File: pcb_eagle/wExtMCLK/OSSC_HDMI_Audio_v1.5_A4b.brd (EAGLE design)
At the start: 29.8 x 25.9 mm, 29 parts, among them U1 PCM1808, U2 74LVC1G34, U3 MK2507SLF

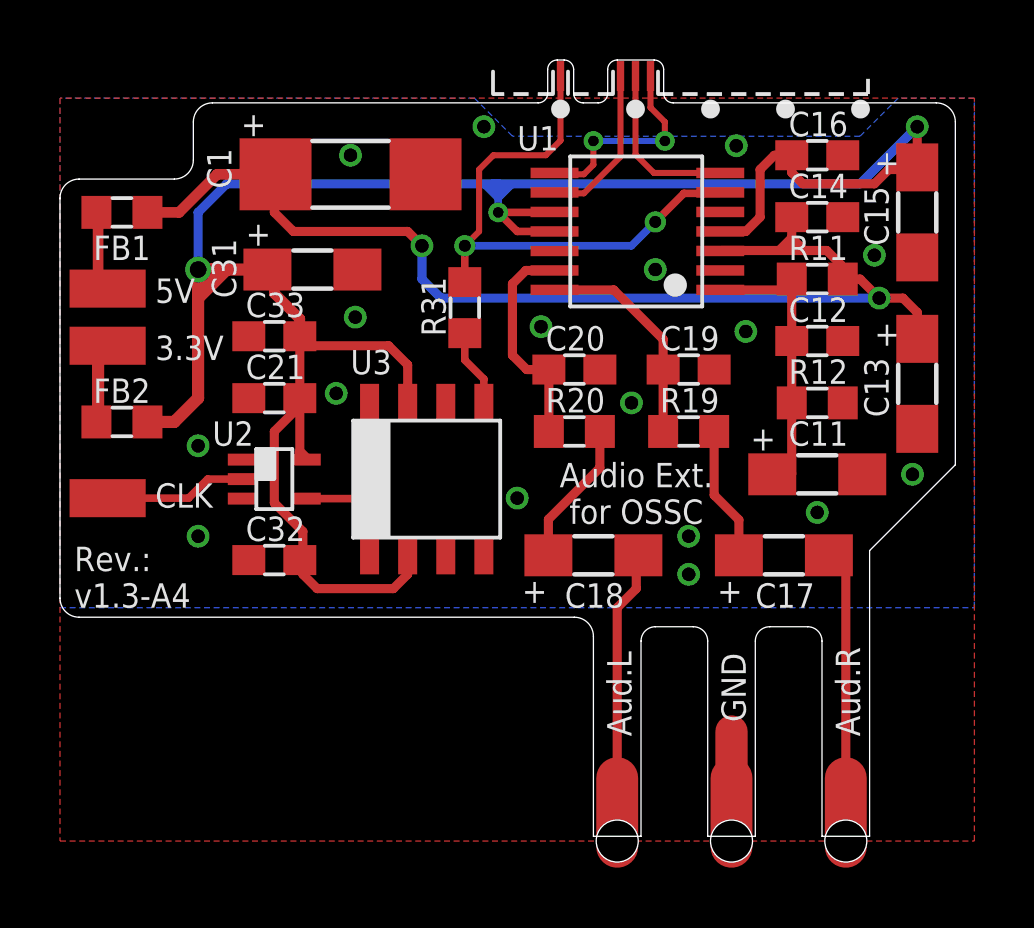
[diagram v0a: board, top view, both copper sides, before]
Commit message: External Masterclock option removed in OSSC firmware v0.75 - PCB files back to A3 - backed up A4 in additional sub-folder
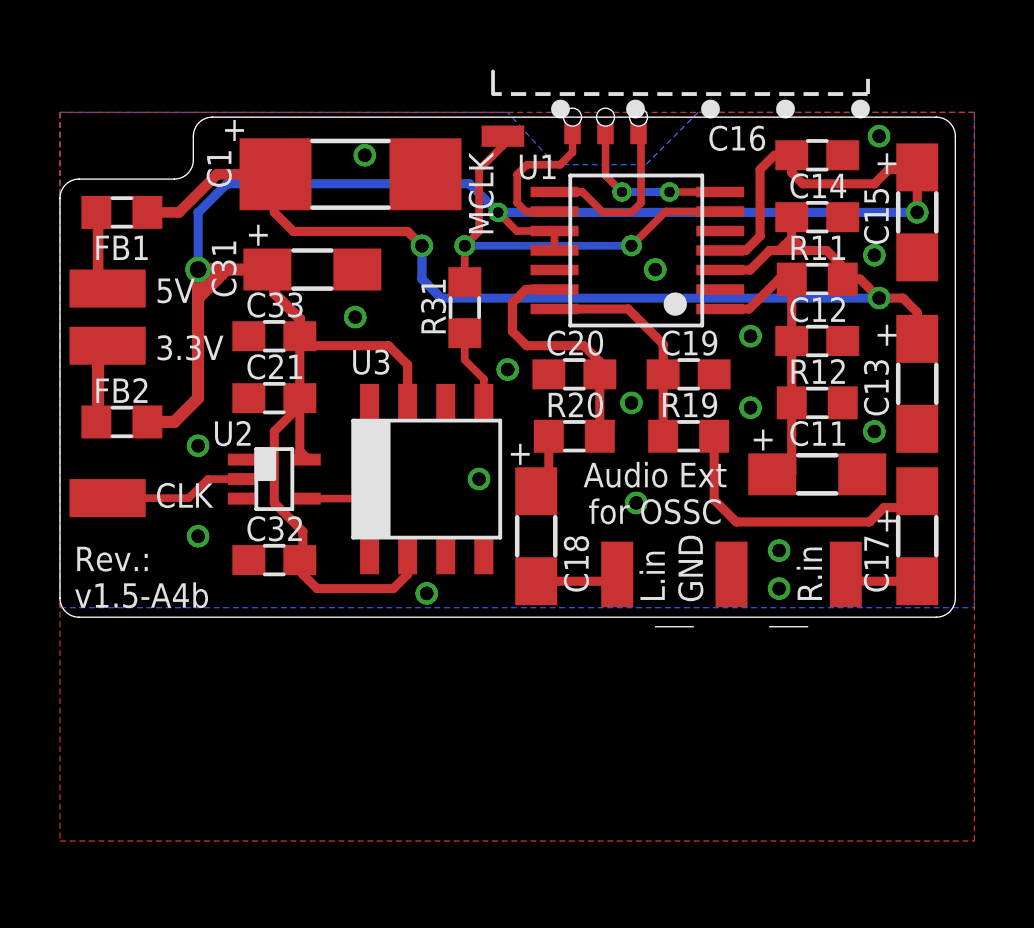
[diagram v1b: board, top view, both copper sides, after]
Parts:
- removed U$4: OSSC_DIY_AUDIO_OVERLAYDIY-V1.3, OSSC_HDMI_Audio:OSSC_OVERLAY_V1.3
- added U$1: OSSC_DIY_AUDIO_OVERLAY_WEXTMCLKDIY-V1.5B, OSSC_HDMI_Audio:OSSC_OVERLAY_V1.5B_WEXTMCLK
- moved C17 4.49 mm to (28.6, 10.2), turned to 270 degrees
- moved C18 2.01 mm to (15.9, 10.2), turned to 270 degrees
- moved U1 0.64 mm to (19.2, 19.7)
- moved C19 0.16 mm to (21.0, 15.6)
- moved C20 0.16 mm to (17.1, 15.6), turned to 0 degrees
- moved R19 0.16 mm to (21.0, 13.5)
- moved R20 0.16 mm to (17.1, 13.5), turned to 180 degrees
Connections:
- net GND: now also U$1.4; no longer U$4.4
- net N$1: now also U$1.6; no longer U$4.6
- net N$13: now also U$1.10; no longer U$4.10
- net N$14: now also U$1.11; no longer U$4.11
- net N$15: now also U$1.9; no longer U$4.9
- net N$17: now also U$1.5; no longer U$4.5
- net N$2: now also U$1.2; no longer U$4.2
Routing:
- net N$2: track 8.81 -> 2.48 mm
- net N$1: track 9.04 -> 2.79 mm
- net N$3: track 4.47 -> 9.85 mm
- net VDD: track 80.0 -> 75.2 mm
- net N$17: track 18.8 -> 14.4 mm
- net GND: track 3.65 -> 0.00 mm
- net N$6: track 4.84 -> 2.44 mm
- net N$14: track 6.98 -> 5.81 mm, vias 2 -> 0
- net N$5: track 7.44 -> 8.36 mm
- net N$13: track 5.69 -> 5.62 mm, vias 0 -> 2
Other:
- board size 29.8 x 25.9 mm -> 29.8 x 17 mm
- board text added: "Audio Ext for OSSC"
- board text added: "L.in"
- board text added: "MCLK"
- board text added: "R.in"
- board text added: "Rev.: v1.5-A4b"
- board text removed: "Aud.L"
- board text removed: "Aud.R"
- board text removed: "Audio Ext. for OSSC"
- board text removed: "Rev.: v1.3-A4"
